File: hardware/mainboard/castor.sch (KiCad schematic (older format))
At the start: 41 parts, among them Q1 MMBT3904, U3 TL074, U4 74LVC2G74, U5 MCP6001-OT, U6 TL074

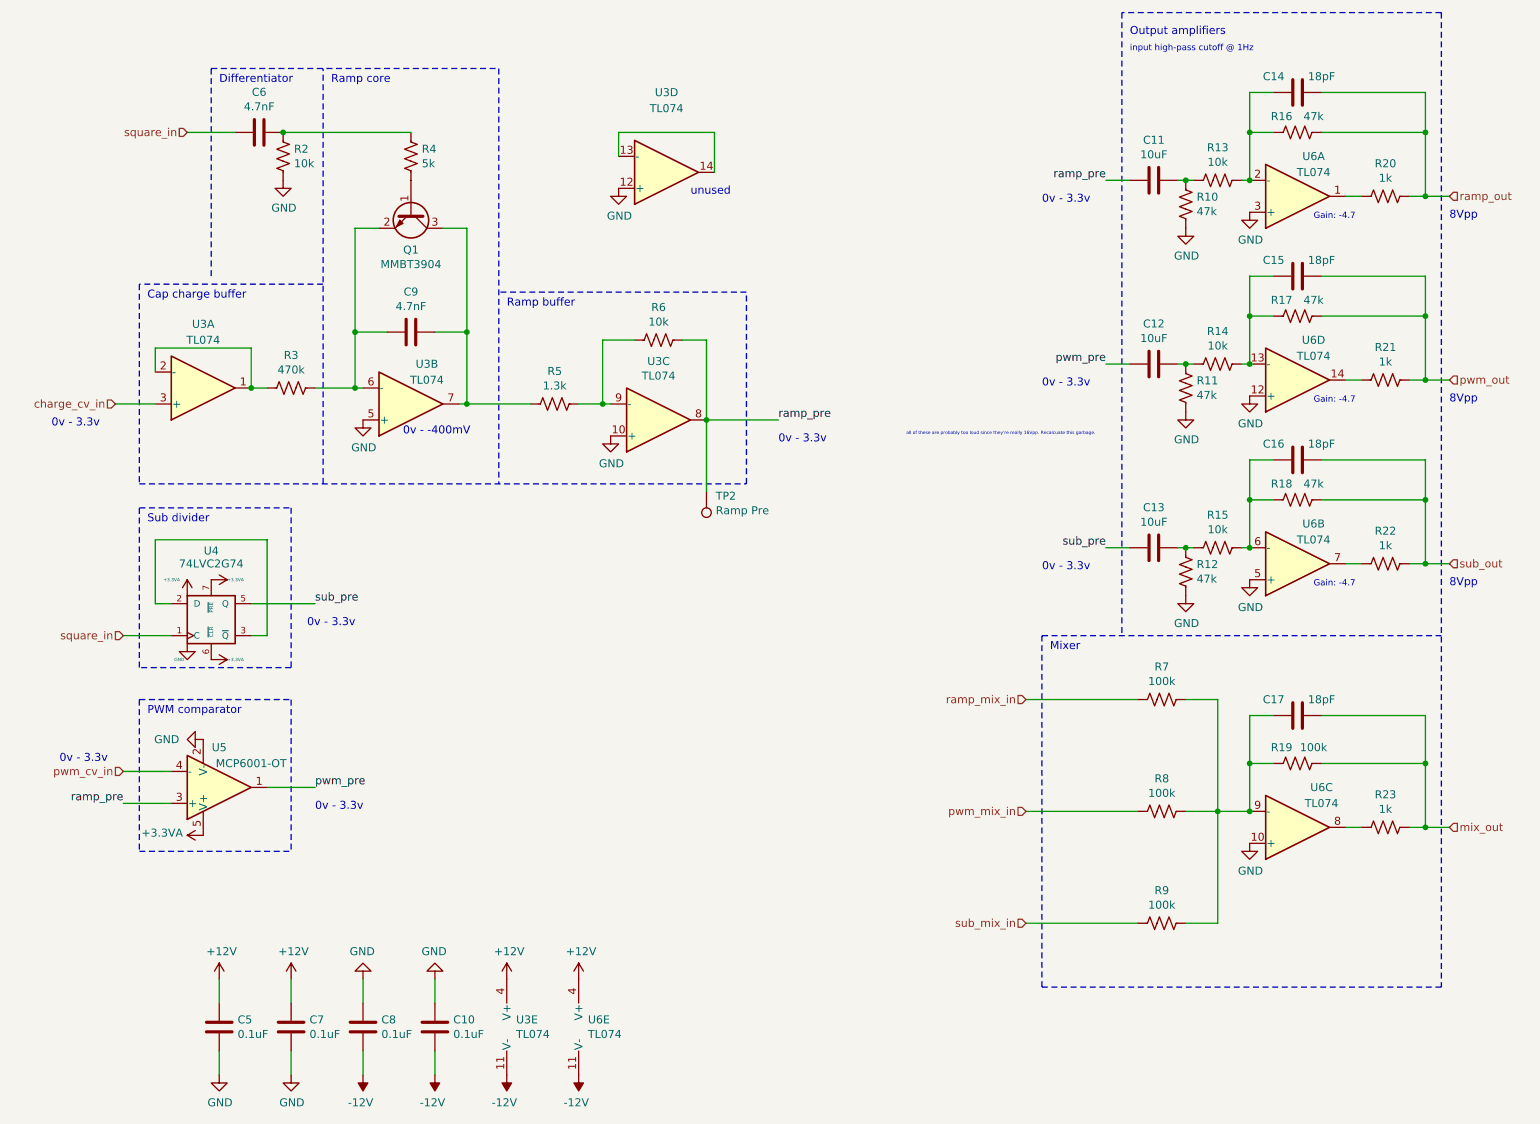
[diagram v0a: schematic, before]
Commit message: First pass layout & component selection for mainboard
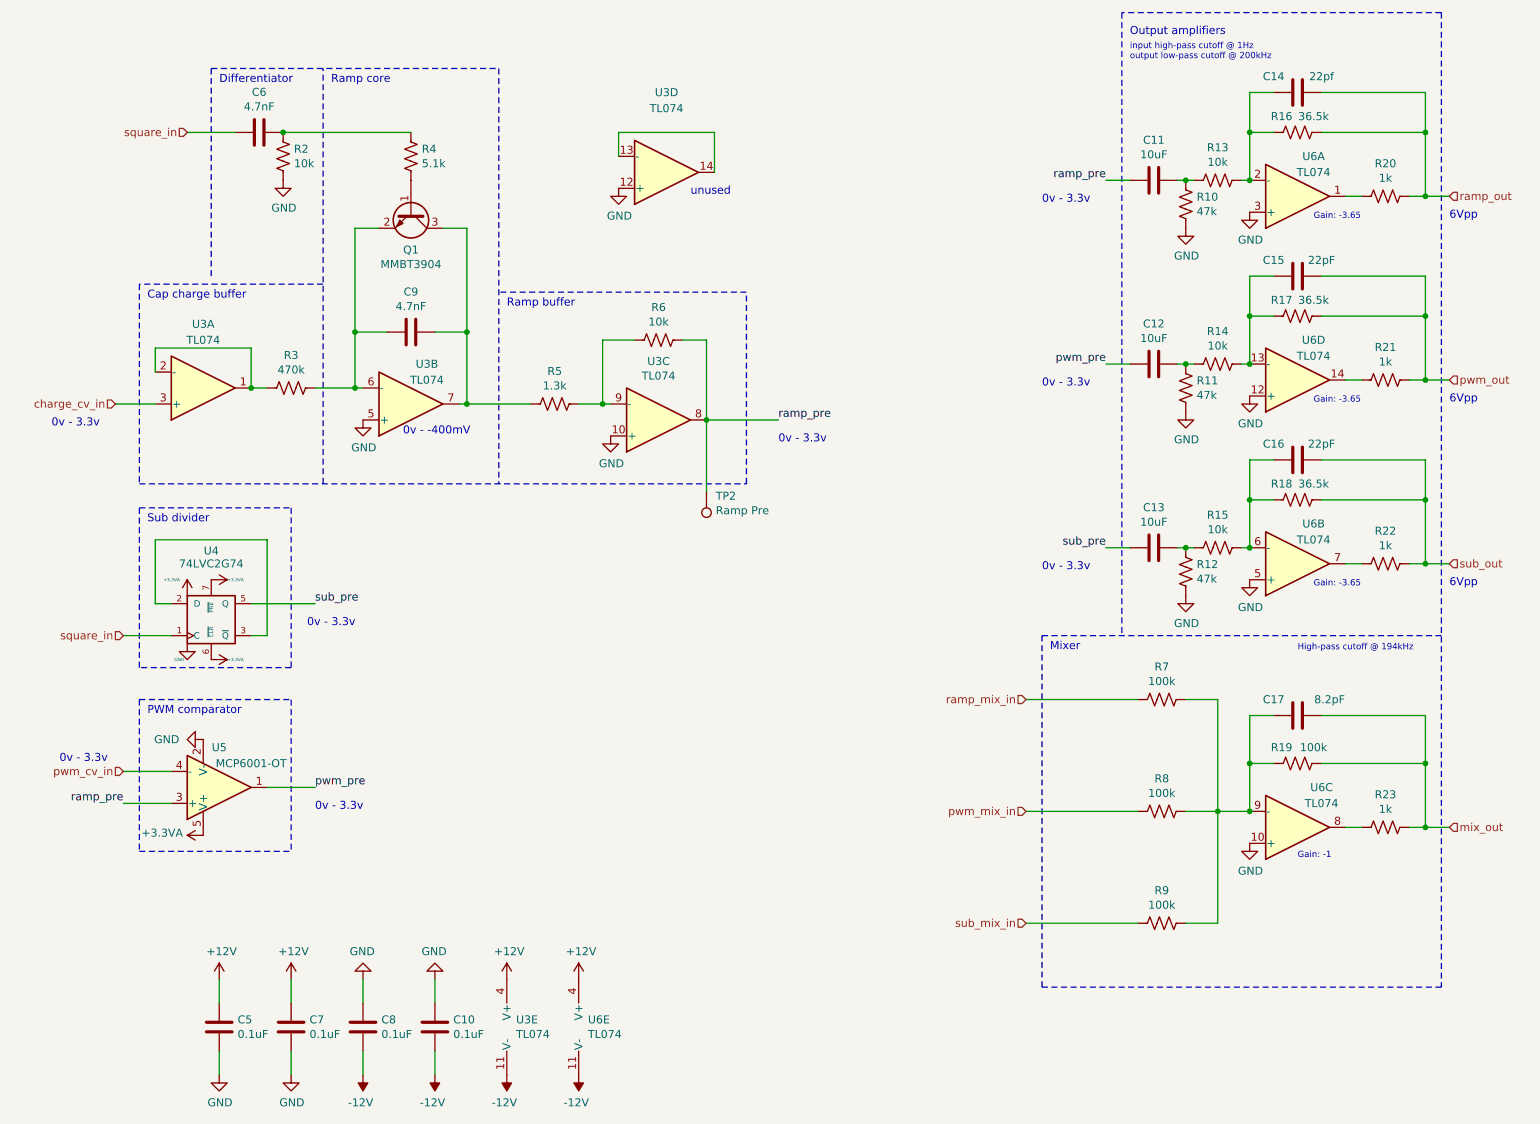
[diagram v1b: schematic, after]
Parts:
- C10, C5, C7, C8: footprint Capacitor_SMD:C_0805_2012Metric_Pad1.15x1.40mm_HandSolder -> Capacitor_SMD:C_0603_1608Metric_Pad1.05x0.95mm_HandSolder; finalized no -> yes
- C11, C12, C13, Q1, U5: finalized no -> yes
- C14: value 18pF -> 22pf; footprint Capacitor_SMD:C_0805_2012Metric_Pad1.15x1.40mm_HandSolder -> Capacitor_SMD:C_0603_1608Metric_Pad1.05x0.95mm_HandSolder; finalized no -> yes; mpn MF-CAP-0603-18pF -> MF-CAP-0603-22pF
- C15, C16: value 18pF -> 22pF; footprint Capacitor_SMD:C_0805_2012Metric_Pad1.15x1.40mm_HandSolder -> Capacitor_SMD:C_0603_1608Metric_Pad1.05x0.95mm_HandSolder; finalized no -> yes; mpn MF-CAP-0603-18pF -> MF-CAP-0603-22pF
- C17: value 18pF -> 8.2pF; footprint Capacitor_SMD:C_0805_2012Metric_Pad1.15x1.40mm_HandSolder -> Capacitor_SMD:C_0603_1608Metric_Pad1.05x0.95mm_HandSolder; finalized no -> yes; mpn MF-CAP-0603-18pF -> CM1885C2A8R2DA16D
- C6, C9: footprint Capacitor_SMD:C_0805_2012Metric_Pad1.15x1.40mm_HandSolder -> Capacitor_SMD:C_0603_1608Metric_Pad1.05x0.95mm_HandSolder; Reqs accurate -> C0G 1%; finalized no -> yes; mpn (none) -> C0603C472F5GACTU
- R10, R11, R12: footprint Resistor_SMD:R_1206_3216Metric_Pad1.42x1.75mm_HandSolder -> Resistor_SMD:R_0603_1608Metric_Pad1.05x0.95mm_HandSolder; Reqs (none) -> 0.5%; finalized no -> yes; mpn ERA8AEB222V -> ERA-3AED473V
- R13, R14, R15, R2, R6: footprint Resistor_SMD:R_1206_3216Metric_Pad1.42x1.75mm_HandSolder -> Resistor_SMD:R_0603_1608Metric_Pad1.05x0.95mm_HandSolder; Reqs (none) -> 1%; finalized no -> yes; mpn ERA8AEB222V -> ERA-3AED103V
- R16, R17, R18: value 47k -> 36.5k; footprint Resistor_SMD:R_1206_3216Metric_Pad1.42x1.75mm_HandSolder -> Resistor_SMD:R_0603_1608Metric_Pad1.05x0.95mm_HandSolder; Reqs (none) -> 0.5%; finalized no -> yes; mpn ERA8AEB222V -> ERA-3AEB3652V
- R19, R7, R8, R9: footprint Resistor_SMD:R_1206_3216Metric_Pad1.42x1.75mm_HandSolder -> Resistor_SMD:R_0603_1608Metric_Pad1.05x0.95mm_HandSolder; Reqs (none) -> 0.5%; finalized no -> yes; mpn ERA8AEB222V -> ERA-3AED104V
- R20, R21, R22, R23: footprint Resistor_SMD:R_1206_3216Metric_Pad1.42x1.75mm_HandSolder -> Resistor_SMD:R_0603_1608Metric_Pad1.05x0.95mm_HandSolder; Reqs (none) -> thin film; finalized no -> yes; mpn ERA8AEB222V -> ERA-3AED102V
- R3: footprint Resistor_SMD:R_1206_3216Metric_Pad1.42x1.75mm_HandSolder -> Resistor_SMD:R_0805_2012Metric_Pad1.15x1.40mm_HandSolder; Reqs (none) -> 0.5%; finalized no -> yes; mpn ERA8AEB222V -> ERA-6AEB474V
- R4: value 5k -> 5.1k; footprint Resistor_SMD:R_1206_3216Metric_Pad1.42x1.75mm_HandSolder -> Resistor_SMD:R_0603_1608Metric_Pad1.05x0.95mm_HandSolder; finalized no -> yes; mpn ERA8AEB222V -> ERA-3AED512V
- R5: footprint Resistor_SMD:R_1206_3216Metric_Pad1.42x1.75mm_HandSolder -> Resistor_SMD:R_0603_1608Metric_Pad1.05x0.95mm_HandSolder; Reqs (none) -> 0.5%; finalized no -> yes; mpn ERA8AEB222V -> ERA-3AEB132V
- U3, U6: finalized no -> yes; mpn TL074 -> TL074CPWR
- U4: footprint Package_SO:VSSOP-8_2.3x2mm_P0.5mm -> Package_SO:TSSOP-8_3x3mm_P0.65mm; finalized no -> yes; mpn 74LVC2G74 -> 74LVC2G74DP,125
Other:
- note added: "6Vpp"
- note added: "Gain: -1"
- note added: "Gain: -3.65"
- note added: "High-pass cutoff @ 194kHz"
- note added: "input high-pass cutoff @ 1Hz\noutput low-pass cutoff @ 200kHz"
- note removed: "8Vpp"
- note removed: "Gain: -4.7"
- note removed: "all of these are probably too loud since they're really 16Vpp. Recalcuate this garbage."
- note removed: "input high-pass cutoff @ 1Hz"

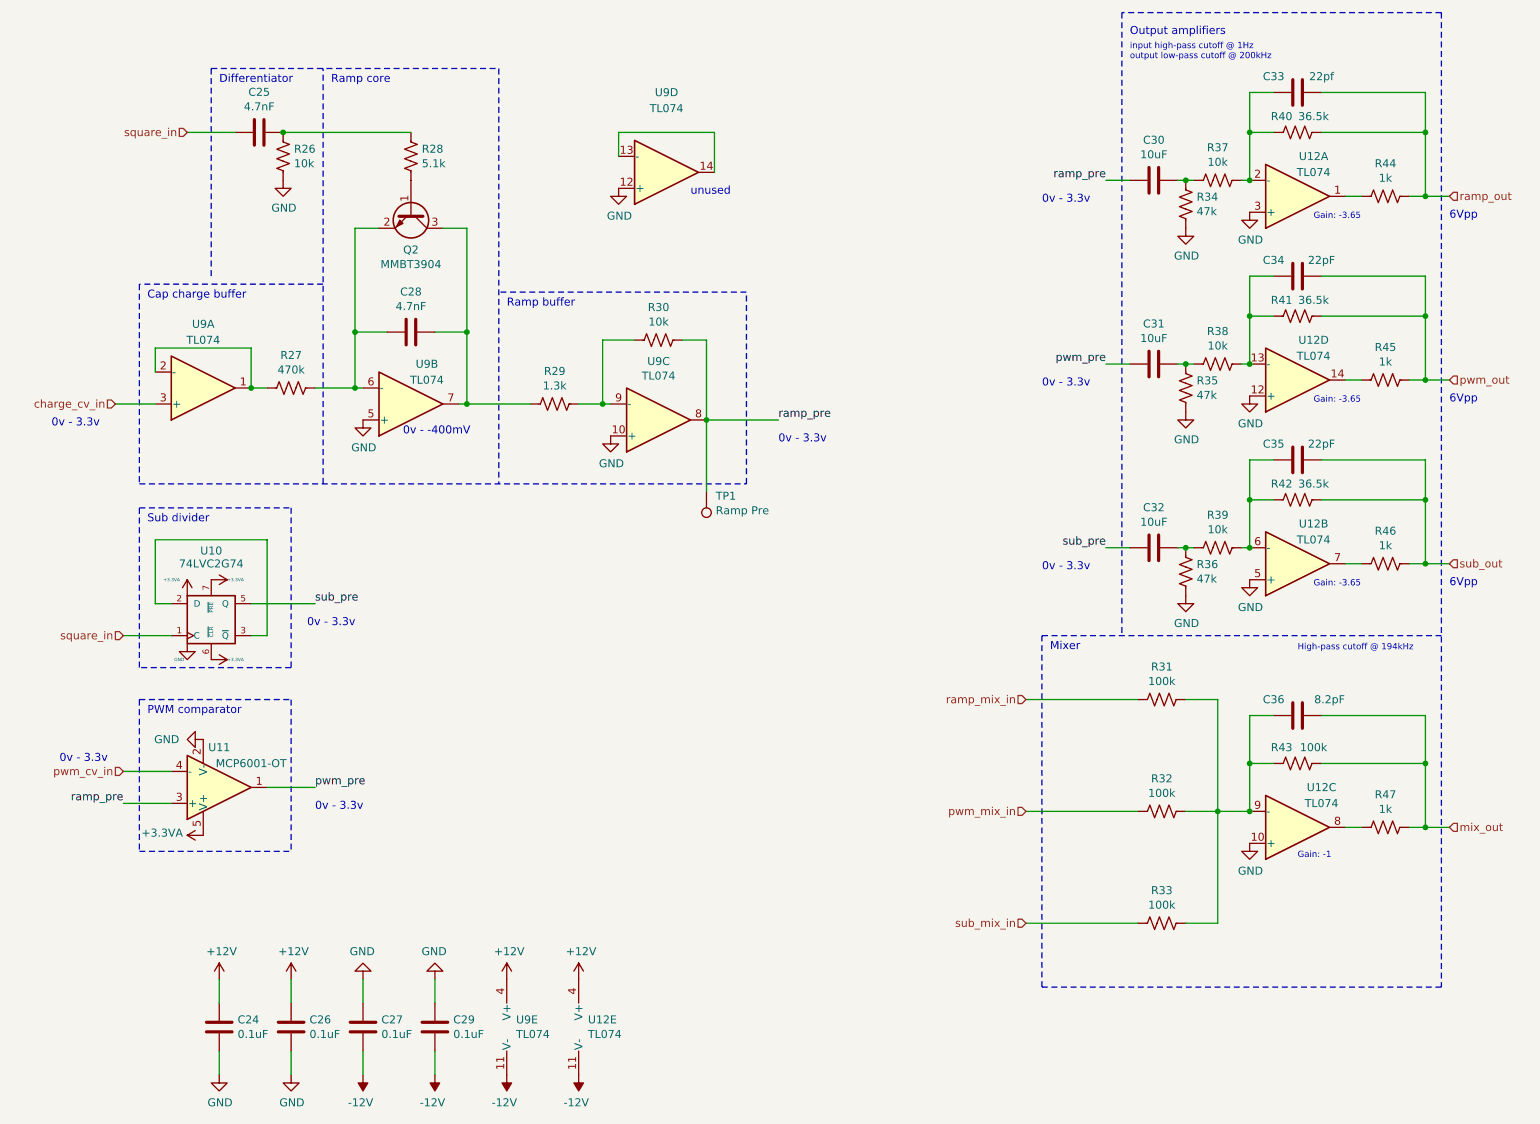
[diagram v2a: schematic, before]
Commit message: Check passive ratings
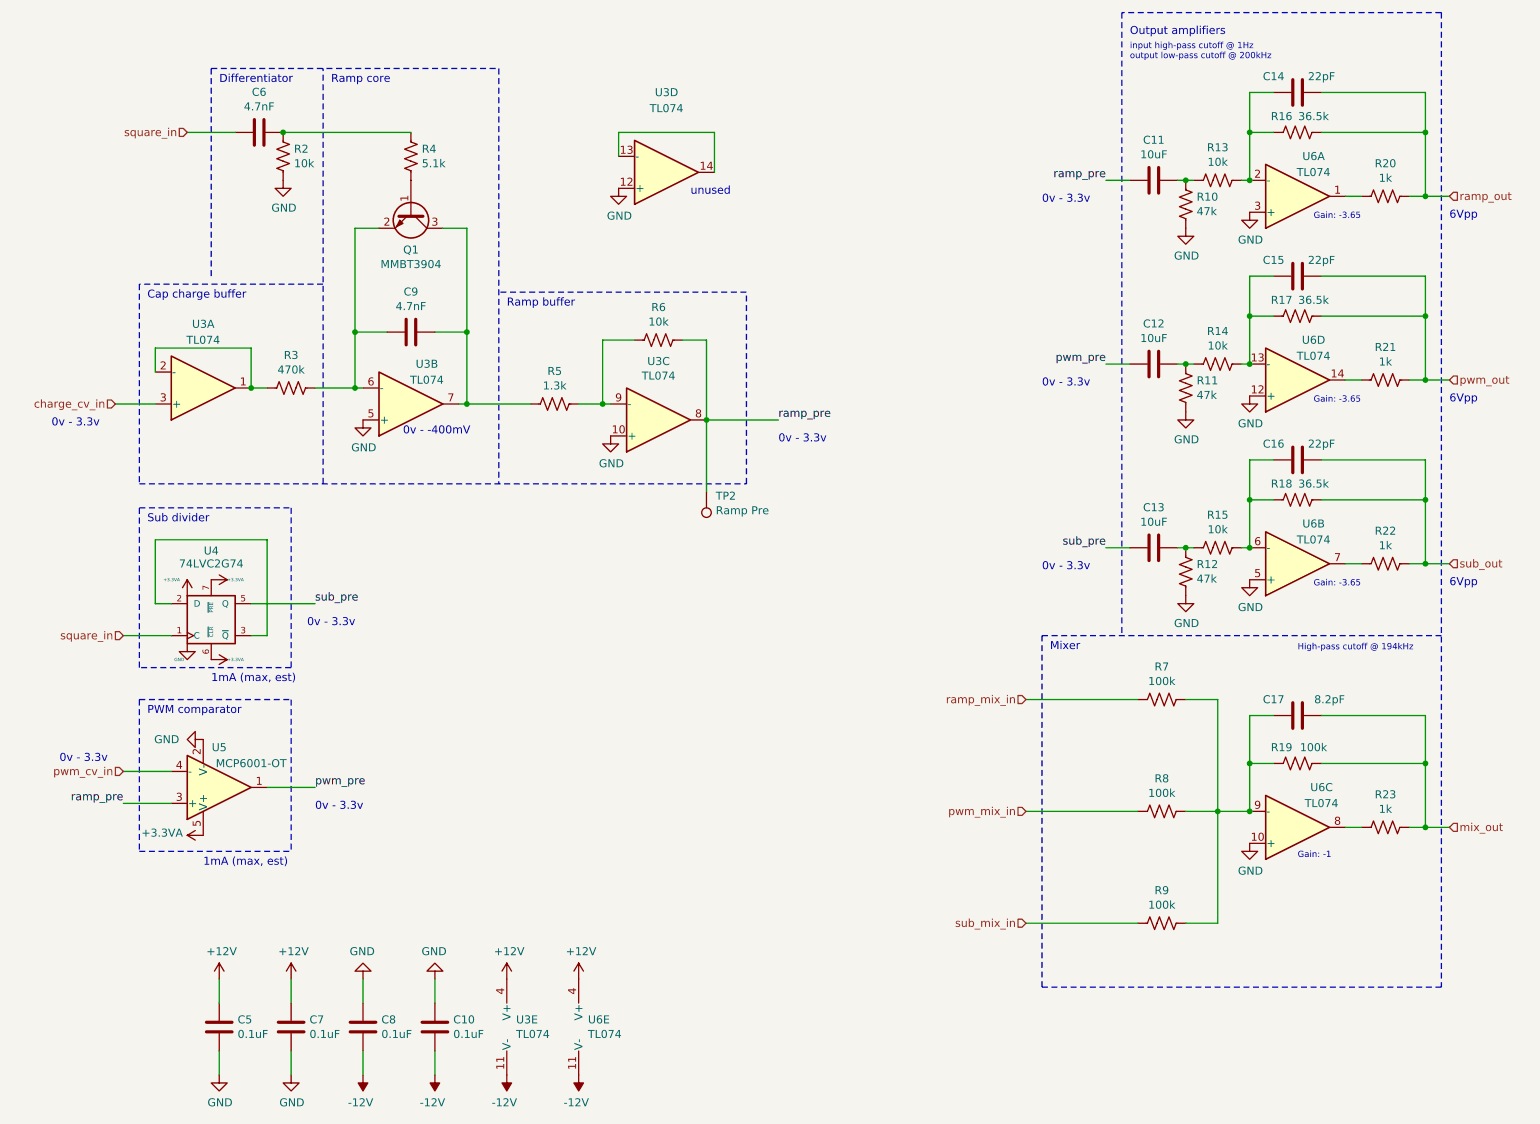
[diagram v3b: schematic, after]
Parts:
- C10, C5, C7, C8: mpn specs (none) -> 10%, 25v
- C11, C12, C13: mpn specs (none) -> 10% 16v
- C14: value 22pf -> 22pF; mpn specs (none) -> 5% 100v
- C15, C16: mpn specs (none) -> 5% 100v
- C17: mpn specs (none) -> +/-0.5pF 100v
- C6: mpn specs (none) -> 1%, 50v
- C9: mpn specs (none) -> 1% 50v
- R10, R11, R12, R13, R14, R15, R16, R17, R18, R19, R2, R20, R21, R22, R23, R3, R4, R5, R6, R7, R8, R9: mpn specs (none) -> 100mW
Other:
- note added: "1mA (max, est)"

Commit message: Bumb schematics after generating gerbers and assigning alt mpns
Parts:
- C10, C5, C7, C8: mpn alt (none) -> GRM188R72A104KA35D
- C11, C12, C13: mpn alt (none) -> GRT31CR61H106ME01L
- C14, C15, C16: mpn alt (none) -> GCM1885C2A220JA16D
- C17: mpn CM1885C2A8R2DA16D -> GCM1885C2A8R2DA16D; mpn specs +/-0.5pF 100v -> (none)
- Q1: mpn alt (none) -> MMBT3904,215
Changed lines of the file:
@@
 F 5 "MF-CAP-1206-10uF" H 7950 1550 50  0001 C CNN "mpn"
 F 6 "10% 16v" H 7950 1550 50  0001 C CNN "mpn specs"
+F 7 "GRT31CR61H106ME01L" H 7950 1550 50  0001 C CNN "mpn alt"
 	1    7950 1550
 	0    1    1    0
@@
 F 5 "MF-CAP-0603-22pF" H 8850 1000 50  0001 C CNN "mpn"
 F 6 "5% 100v" H 8850 1000 50  0001 C CNN "mpn specs"
+F 7 "GCM1885C2A220JA16D" H 8850 1000 50  0001 C CNN "mpn alt"
 	1    8850 1000
 	0    1    1    0
@@
 F 5 "MF-CAP-1206-10uF" H 7950 2700 50  0001 C CNN "mpn"
 F 6 "10% 16v" H 7950 2700 50  0001 C CNN "mpn specs"
+F 7 "GRT31CR61H106ME01L" H 7950 2700 50  0001 C CNN "mpn alt"
 	1    7950 2700
 	0    1    1    0
@@
 F 5 "MF-CAP-0603-22pF" H 8850 2150 50  0001 C CNN "mpn"
 F 6 "5% 100v" H 8850 2150 50  0001 C CNN "mpn specs"
+F 7 "GCM1885C2A220JA16D" H 8850 2150 50  0001 C CNN "mpn alt"
 	1    8850 2150
 	0    1    1    0
@@
 F 5 "MF-CAP-0603-0.1uF" H 3450 6850 50  0001 C CNN "mpn"
 F 6 "10%, 25v" H 3450 6850 50  0001 C CNN "mpn specs"
+F 7 "GRM188R72A104KA35D" H 3450 6850 50  0001 C CNN "mpn alt"
 	1    3450 6850
 	1    0    0    -1
@@
 F 5 "MF-CAP-0603-0.1uF" H 3000 6850 50  0001 C CNN "mpn"
 F 6 "10%, 25v" H 3000 6850 50  0001 C CNN "mpn specs"
+F 7 "GRM188R72A104KA35D" H 3000 6850 50  0001 C CNN "mpn alt"
 	1    3000 6850
 	1    0    0    -1
@@
 F 5 "MF-CAP-0603-0.1uF" H 2550 6850 50  0001 C CNN "mpn"
 F 6 "10%, 25v" H 2550 6850 50  0001 C CNN "mpn specs"
+F 7 "GRM188R72A104KA35D" H 2550 6850 50  0001 C CNN "mpn alt"
 	1    2550 6850
 	1    0    0    -1
@@
 F 5 "MF-CAP-0603-0.1uF" H 2100 6850 50  0001 C CNN "mpn"
 F 6 "10%, 25v" H 2100 6850 50  0001 C CNN "mpn specs"
+F 7 "GRM188R72A104KA35D" H 2100 6850 50  0001 C CNN "mpn alt"
 	1    2100 6850
 	1    0    0    -1
@@
 F 3 "~" H 8850 4900 50  0001 C CNN
 F 4 "yes" H 8850 4900 50  0001 C CNN "finalized"
-F 5 "CM1885C2A8R2DA16D" H 8850 4900 50  0001 C CNN "mpn"
-F 6 "+/-0.5pF 100v" H 8850 4900 50  0001 C CNN "mpn specs"
+F 5 "GCM1885C2A8R2DA16D" H 8850 4900 50  0001 C CNN "mpn"
+F 6 "" H 8850 4900 50  0001 C CNN "mpn specs"
 	1    8850 4900
 	0    1    1    0
@@
 F 4 "yes" H 3300 1750 50  0001 C CNN "finalized"
 F 5 "MF-DSC-SOT233-MMBT3904" H 3300 1750 50  0001 C CNN "mpn"
+F 6 "MMBT3904,215" H 3300 1750 50  0001 C CNN "mpn alt"
 	1    3300 1750
 	0    1    1    0
@@
 F 5 "MF-CAP-0603-22pF" H 8850 3300 50  0001 C CNN "mpn"
 F 6 "5% 100v" H 8850 3300 50  0001 C CNN "mpn specs"
+F 7 "GCM1885C2A220JA16D" H 8850 3300 50  0001 C CNN "mpn alt"
 	1    8850 3300
 	0    1    1    0
@@
 F 5 "MF-CAP-1206-10uF" H 7950 3850 50  0001 C CNN "mpn"
 F 6 "10% 16v" H 7950 3850 50  0001 C CNN "mpn specs"
+F 7 "GRT31CR61H106ME01L" H 7950 3850 50  0001 C CNN "mpn alt"
 	1    7950 3850
 	0    1    1    0
